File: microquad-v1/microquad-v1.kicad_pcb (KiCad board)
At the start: 2 copper layers, 53.3 x 53.3 mm, 79 parts, among them J1 USB_microB_2040002-1, M1 Motor_DC, M2 Motor_DC, M3 Motor_DC, M4 Motor_DC, M5 Motor_DC, M6 Motor_DC, Q1 Q_NMOS_GSD, Q2 Q_NMOS_GSD, Q3 Q_NMOS_GSD, Q4 Q_NMOS_GSD, Q5 Q_NMOS_GSD, Q6 Q_NMOS_GSD, SW1 SERIAL, SW2 POWER, SW3 RESET, U1 ATMEGA328PB, U2 MCP1703A-3302_SOT23, U3 FT230XS, U4 MCP73812T, U5 MAX6333UR18D3

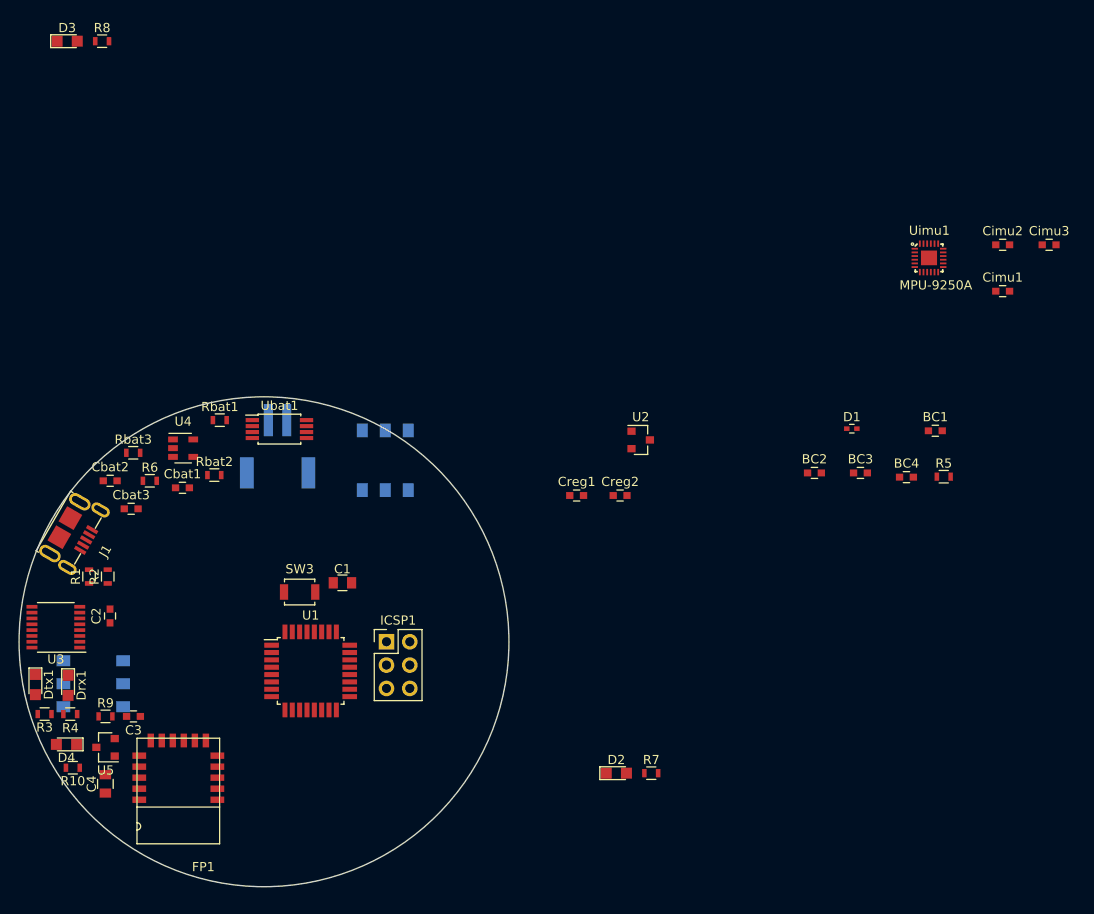
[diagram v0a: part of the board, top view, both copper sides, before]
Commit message: All non-motor components placed on board
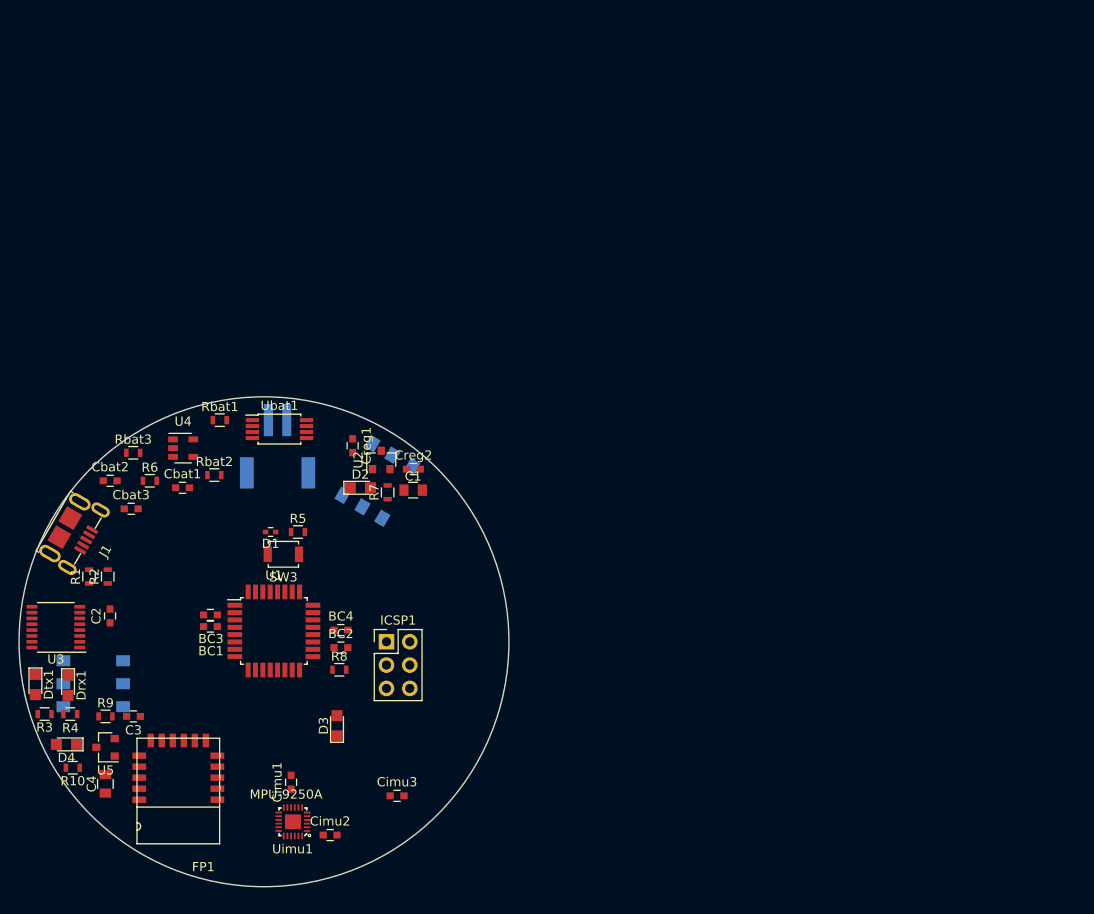
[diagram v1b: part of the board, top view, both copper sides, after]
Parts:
- moved Cimu2 97.4 mm to (153.2, 129.0)
- moved Cimu1 94.1 mm to (149.0, 123.2), turned to 90 degrees
- moved Cimu3 93.0 mm to (160.5, 124.7)
- moved Uimu1 92.6 mm to (149.2, 127.5), turned to 180 degrees
- moved BC1 81.8 mm to (140.2, 106.3), turned to 180 degrees
- moved D3 80.1 mm to (154.0, 117.1), turned to 90 degrees
- moved R8 73.2 mm to (154.2, 111.0)
- moved BC3 72.4 mm to (140.2, 105.0), turned to 180 degrees
- moved R5 70.6 mm to (149.8, 96.0)
- moved D1 64.3 mm to (146.8, 96.0), turned to 180 degrees
- moved BC4 63.8 mm to (154.4, 106.7)
- moved BC2 55.0 mm to (154.4, 108.6)
- moved R7 41.9 mm to (159.5, 91.7), turned to 90 degrees
- moved D2 41.7 mm to (156.5, 91.2)
- moved U2 28.3 mm to (158.8, 88.2), turned to 90 degrees
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
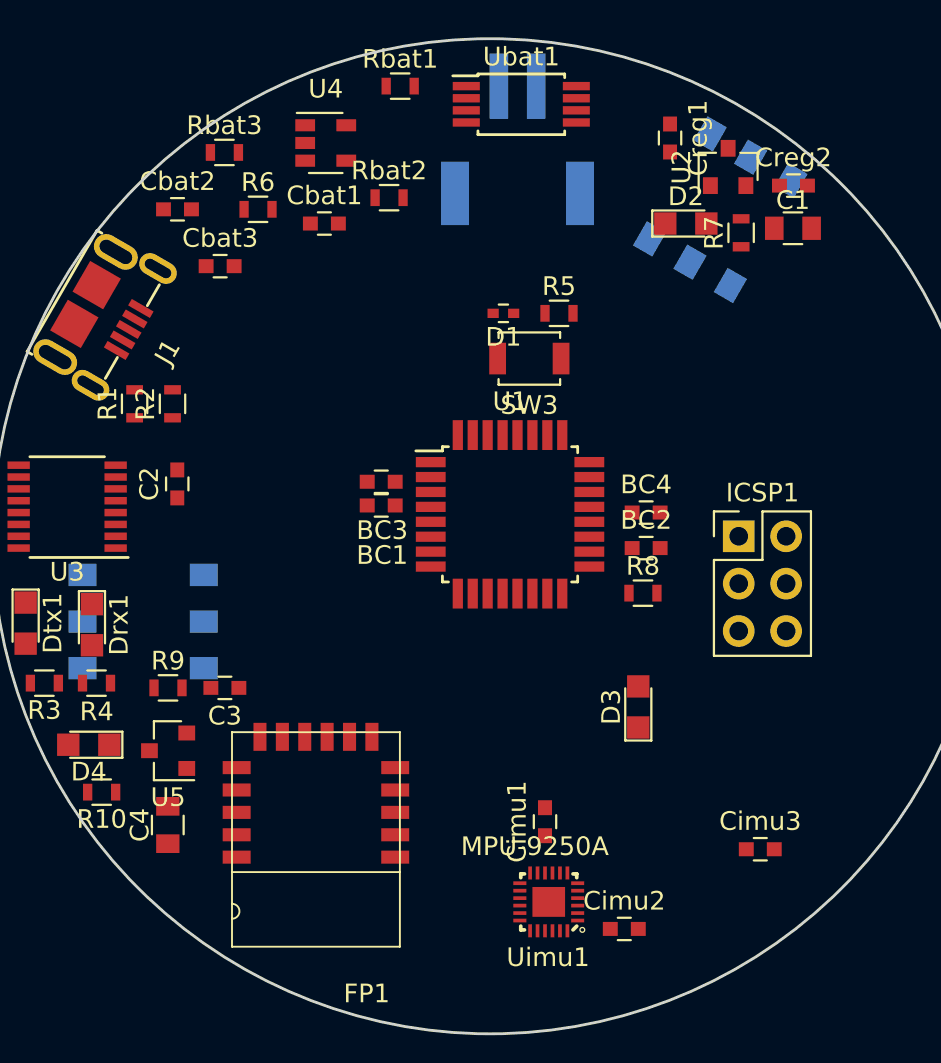
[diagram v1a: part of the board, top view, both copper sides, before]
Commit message: Initial power routing to all major chips
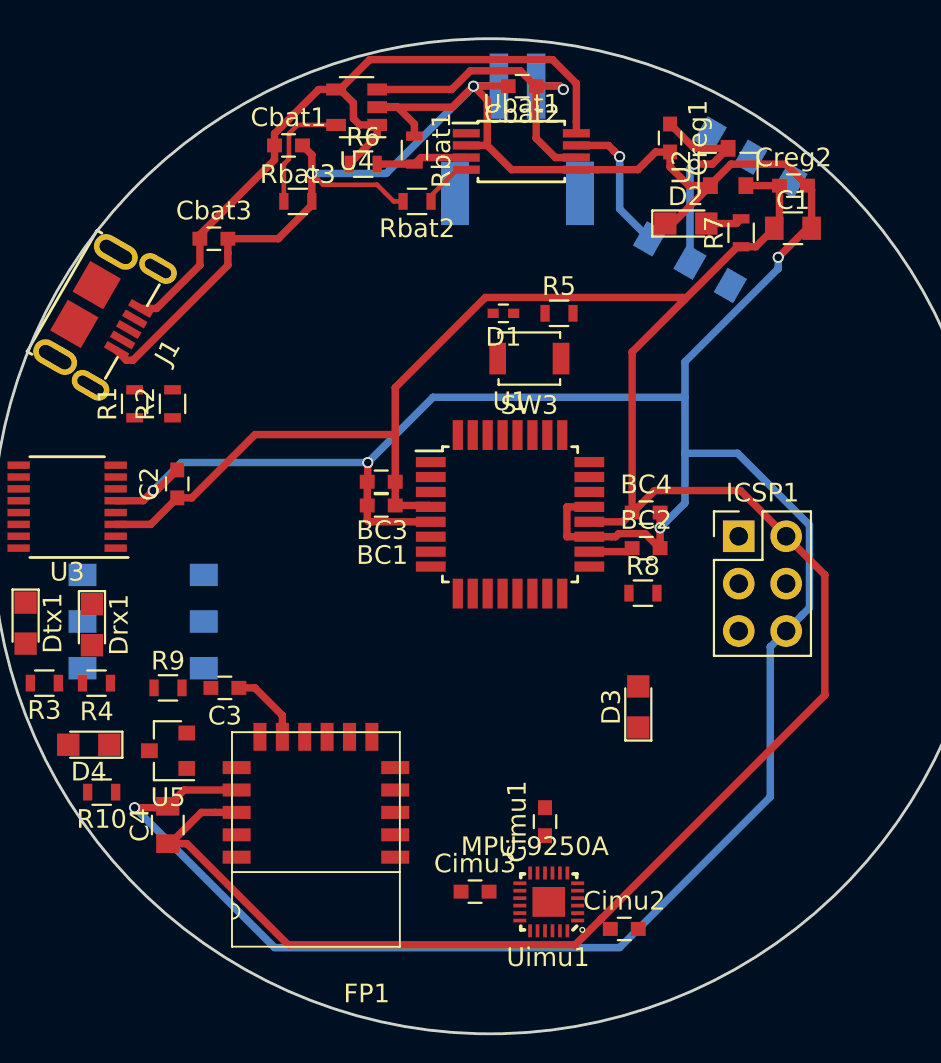
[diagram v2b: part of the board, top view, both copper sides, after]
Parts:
- moved Cbat2 19.6 mm to (147.8, 83.8), turned to 180 degrees
- moved Cimu3 15.5 mm to (145.2, 127.0)
- moved R6 6.13 mm to (139.2, 88.0)
- moved Rbat3 4.73 mm to (135.8, 90.0)
- moved Cbat1 4.61 mm to (135.2, 87.0)
- moved Rbat1 3.51 mm to (142.0, 87.2), turned to 270 degrees
- moved U4 2.53 mm to (138.9, 85.0), turned to 180 degrees
- moved Ubat1 2.53 mm to (147.7, 87.3)
- moved Rbat2 1.51 mm to (142.1, 90.0), turned to 180 degrees
- moved Cbat3 1.51 mm to (131.2, 92.0)
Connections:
- BC4 pad 1: /ATMEGA power/AREF -> +3V3
- U1 pad 20: /ATMEGA power/AREF -> +3V3
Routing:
- net GND: track 0.00 -> 217.8 mm, vias 0 -> 7
- net +3V3: track 0.00 -> 137.4 mm
- net /USB interface/5V: track 0.00 -> 40.4 mm
- net Net-(Cbat2-Pad1): track 0.00 -> 17.7 mm, vias 0 -> 1
- net /VBAT: track 0.00 -> 11.2 mm, vias 0 -> 1
- net /Battery/Vout: track 0.00 -> 7.64 mm, vias 0 -> 1
- net Net-(Rbat3-Pad1): track 0.00 -> 6.47 mm
- net Net-(R6-Pad2): track 0.00 -> 4.92 mm
- net Net-(C3-Pad1): track 0.00 -> 4.09 mm
- net Net-(Rbat2-Pad1): track 0.00 -> 2.78 mm
- net Net-(D2-Pad2): track 0.00 -> 1.97 mm
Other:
- net class Power added: clearance 0.2, trace_width 0.4, via_dia 0.6, via_drill 0.4

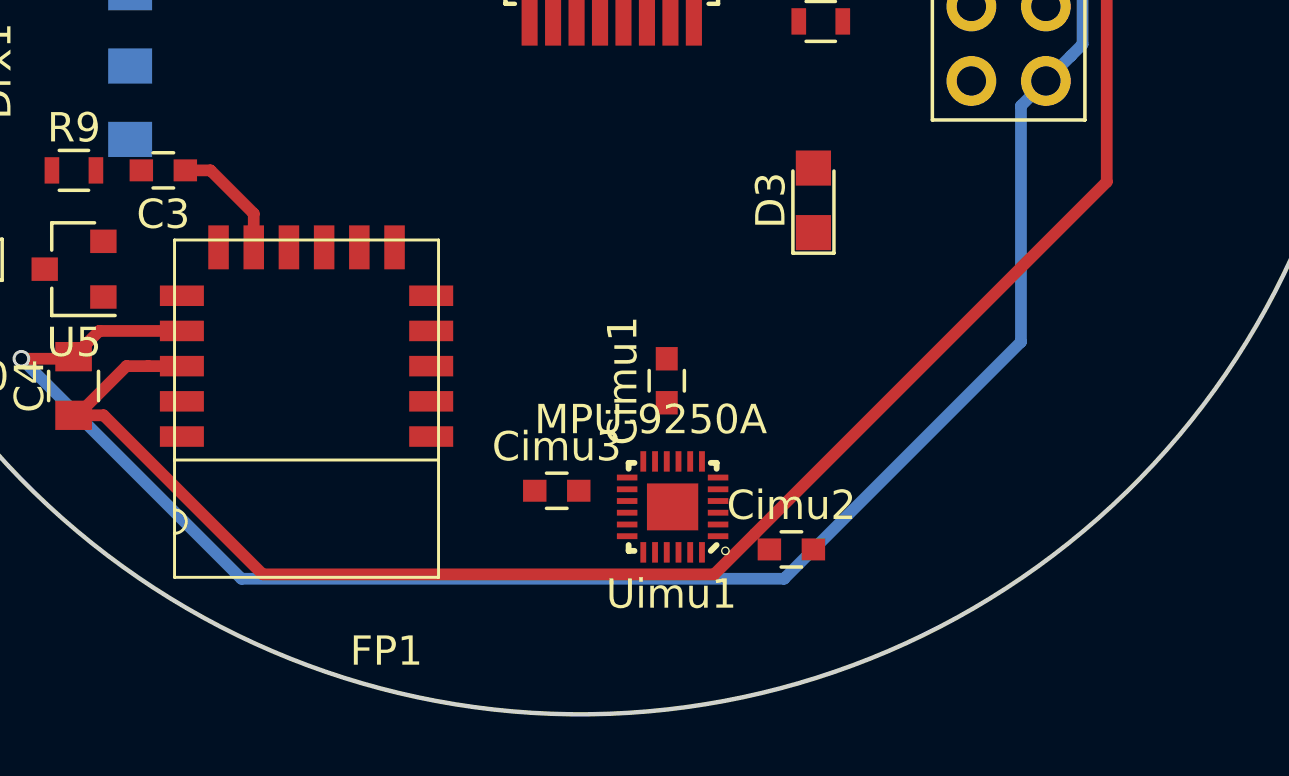
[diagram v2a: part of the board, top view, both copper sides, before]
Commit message: Handled some wire routing for IMU
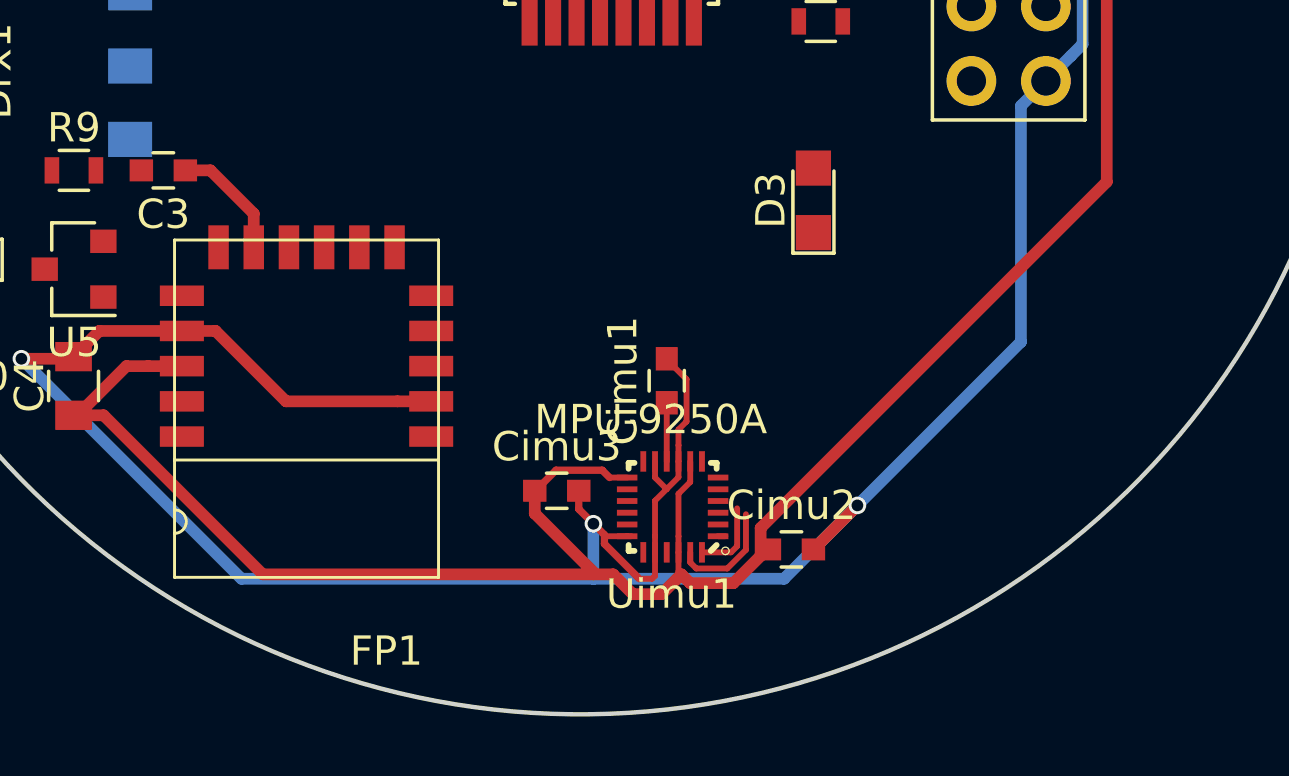
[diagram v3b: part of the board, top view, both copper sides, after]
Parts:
- Uimu1: footprint imulogger2:QFN40P300X300X105-25N -> QFN40P300X300X105-25N
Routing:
- net GND: track 217.8 -> 245.9 mm, vias 7 -> 9
- net +3V3: track 137.4 -> 150.3 mm
- net /IMU/SCL: track 0.00 -> 3.81 mm
- net /IMU/SDA: track 0.00 -> 2.58 mm
- net Net-(Cimu1-Pad1): track 0.00 -> 2.00 mm
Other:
- net class Micro added: clearance 0.1, trace_width 0.2, via_dia 0.6, via_drill 0.4

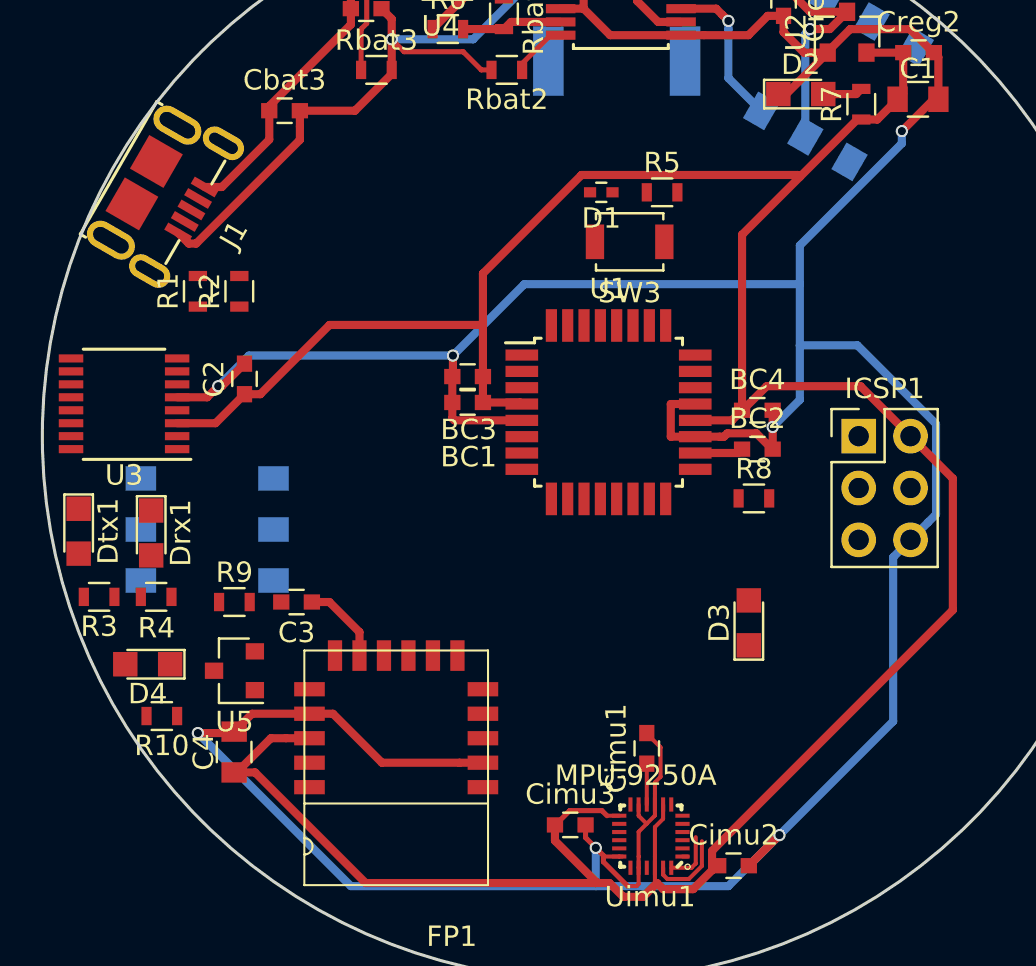
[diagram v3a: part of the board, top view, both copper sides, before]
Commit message: Finished routing most of the top side
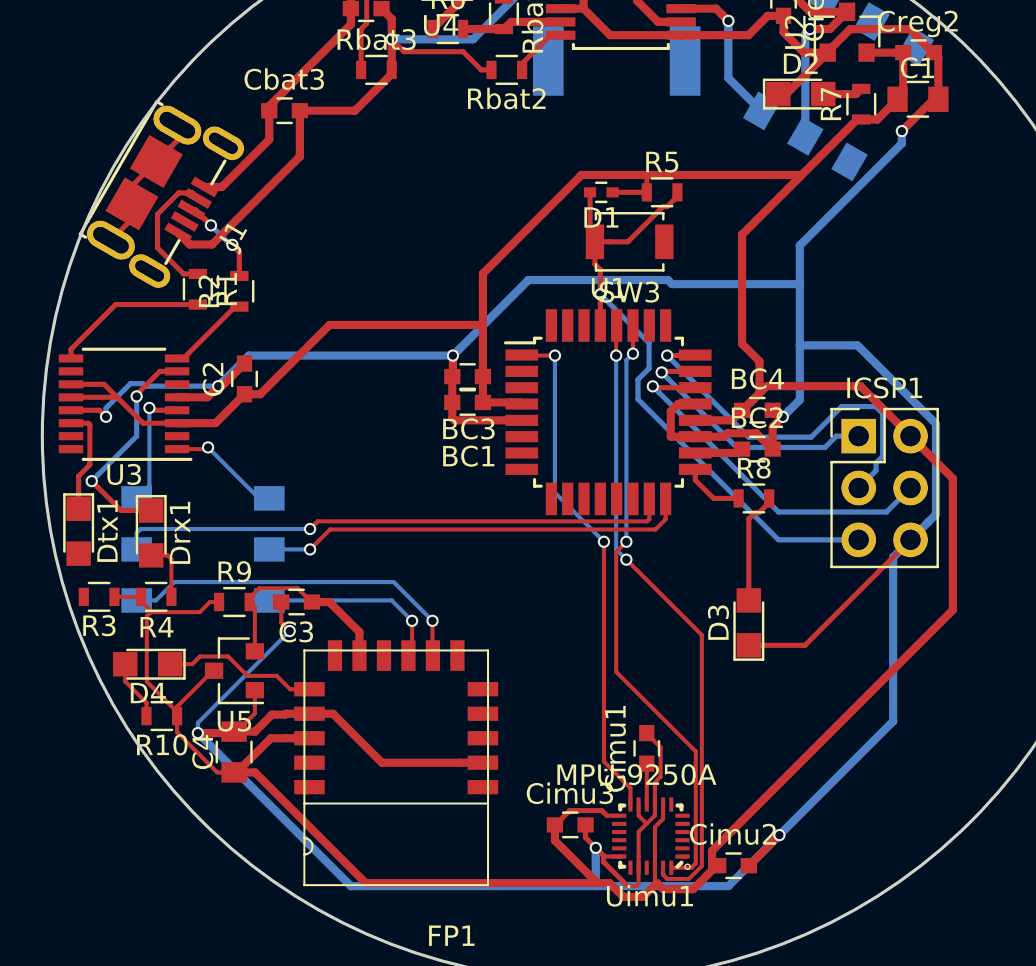
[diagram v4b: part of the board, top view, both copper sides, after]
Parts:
- moved SW1 7.47 mm to (130.5, 111.0), turned to 180 degrees
- moved R1 0.10 mm to (127.0, 100.8), turned to 270 degrees
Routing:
- net GND: track 245.9 -> 283.7 mm, vias 9 -> 11
- net /RESET: track 0.00 -> 31.9 mm, vias 0 -> 1
- net +3V3: track 150.3 -> 181.8 mm
- net Net-(SW1-Pad5): track 0.00 -> 27.2 mm, vias 0 -> 1
- net /IMU/SDA: track 2.58 -> 29.6 mm, vias 0 -> 2
- net /IMU/SCL: track 3.81 -> 30.8 mm, vias 0 -> 2
- net /IMU_INT: track 0.00 -> 25.2 mm, vias 0 -> 2
- net Net-(SW1-Pad2): track 0.00 -> 21.0 mm, vias 0 -> 1
- net Net-(ICSP1-Pad3): track 0.00 -> 18.5 mm, vias 0 -> 1
- net Net-(ICSP1-Pad4): track 0.00 -> 17.8 mm, vias 0 -> 1
- net /BLE/RX: track 0.00 -> 17.4 mm, vias 0 -> 1
- net Net-(ICSP1-Pad1): track 0.00 -> 13.1 mm, vias 0 -> 1
- net Net-(Drx1-Pad1): track 0.00 -> 11.1 mm, vias 0 -> 2
- net /BLE/TX: track 0.00 -> 9.19 mm, vias 0 -> 1
- net Net-(D4-Pad1): track 0.00 -> 7.65 mm
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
